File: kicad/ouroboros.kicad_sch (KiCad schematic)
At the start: 121 parts, among them J1 Eurorack Mono Jack, J10 Conn_01x03_Male, J11 Eurorack Mono Jack, J12 Eurorack Mono Jack, J13 Eurorack Mono Jack, J14 Eurorack Mono Jack, J19 Eurorack Mono Jack, J2 Eurorack Mono Jack, J20 Eurorack Mono Jack, J21 Eurorack Mono Jack, J22 Eurorack Mono Jack, J23 Eurorack Mono Jack, J24 Eurorack Mono Jack, J25 Eurorack Mono Jack, J26 Eurorack Mono Jack, J27 Eurorack Mono Jack, J28 Conn_01x06_Male, J29 Conn_01x04_Male, J3 Eurorack Mono Jack, J30 Conn_01x04_Male, J31 Conn_01x04_Male, J32 Conn_01x06_Male, J33 Conn_01x04_Male, J34 Conn_01x08_Male, J35 Conn_01x08_Male, J36 Eurorack Power Small, J38 Conn_02x04_Odd_Even, J4 Eurorack Mono Jack, J40 Conn_01x08_Female, J41 Conn_01x08_Female, J42 Conn_01x04_Female, J43 Conn_01x06_Female, J44 Conn_01x04_Female, J45 Conn_01x04_Female, J46 Conn_01x04_Female, J47 Conn_01x06_Female, J5 Eurorack Mono Jack, J6 Eurorack Mono Jack, J7 Eurorack Mono Jack, J8 Eurorack Mono Jack, J9 Eurorack Mono Jack, U1 TL074, U8 L78L05_TO92

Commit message: Updating pcb after tweaks
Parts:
- added R134: 100k, Rumblesan_Standard_Parts:R_Axial_DIN0207_L6.3mm_D2.5mm_P10.16mm_Horizontal, symbol Rumblesan_Standard_Parts:R
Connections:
- net VCC: now also R134.1; no longer RV20.1
- new net: R134.2, RV20.1
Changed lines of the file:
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@@
 	(wire
 		(pts
+			(xy 307.34 57.15) (xy 307.34 60.96)
+		)
+		(stroke
+			(width 0)
+			(type default)
+		)
+	)
+	(wire
+		(pts
 			(xy 200.66 45.72) (xy 200.66 95.25)
 		)
@@
 	(wire
 		(pts
-			(xy 307.34 58.42) (xy 307.34 60.96)
+			(xy 307.34 48.26) (xy 307.34 49.53)
 		)
 		(stroke
@@
 		)
 		(property "Name" "VCA Level CV"
-			(at 252.73 203.2 0)
+			(at 242.316 198.12 90)
 			(effects
 				(font
@@
 	(symbol
 		(lib_id "power:VCC")
-		(at 307.34 58.42 0)
+		(at 307.34 48.26 0)
 		(unit 1)
 		(exclude_from_sim no)
@@
 		(fields_autoplaced yes)
 		(property "Reference" "#PWR050"
-			(at 307.34 62.23 0)
+			(at 307.34 52.07 0)
 			(effects
 				(font
@@
 		)
 		(property "Value" "VCC"
-			(at 307.34 54.8442 0)
+			(at 307.34 44.6842 0)
 			(effects
 				(font
@@
 		)
 		(property "Footprint" ""
-			(at 307.34 58.42 0)
+			(at 307.34 48.26 0)
 			(effects
 				(font
@@
 		)
 		(property "Datasheet" ""
-			(at 307.34 58.42 0)
+			(at 307.34 48.26 0)
 			(effects
 				(font
@@
 		)
 		(property "Description" "Power symbol creates a global label with name \"VCC\""
-			(at 307.34 58.42 0)
+			(at 307.34 48.26 0)
 			(effects
 				(font
@@
 	)
 	(symbol
+		(lib_id "Rumblesan_Standard_Parts:R")
+		(at 307.34 53.34 0)
+		(mirror y)
+		(unit 1)
+		(exclude_from_sim no)
+		(in_bom yes)
+		(on_board yes)
+		(dnp no)
+		(property "Reference" "R134"
+			(at 300.228 53.086 0)
+			(effects
+				(font
+					(size 1.27 1.27)
+				)
+				(justify right)
+			)
+		)
+		(property "Value" "100k"
+			(at 300.228 51.308 0)
+			(effects
+				(font
+					(size 1.27 1.27)
+				)
+				(justify right)
+			)
+		)
+		(property "Footprint" "Rumblesan_Standard_Parts:R_Axial_DIN0207_L6.3mm_D2.5mm_P10.16mm_Horizontal"
+			(at 304.8 55.88 90)
+			(effects
+				(font
+					(size 1.27 1.27)
+				)
+				(hide yes)
+			)
+		)
+		(property "Datasheet" "~"
+			(at 300.99 53.34 90)
+			(effects
+				(font
+					(size 1.27 1.27)
+				)
+				(hide yes)
+			)
+		)
+		(property "Description" "Resistor"
+			(at 307.34 53.34 0)
+			(effects
+				(font
+					(size 1.27 1.27)
+				)
+				(hide yes)
+			)
+		)
+		(property "Tolerance" "1%"
+			(at 302.26 59.69 90)
+			(effects
+				(font
+					(size 1.27 1.27)
+				)
+				(hide yes)
+			)
+		)
+		(property "Power" "0.5W"
+			(at 302.26 45.72 90)
+			(effects
+				(font
+					(size 1.27 1.27)
+				)
+				(hide yes)
+			)
+		)
+		(property "Spec" "metal film"
+			(at 302.26 53.34 90)
+			(effects
+				(font
+					(size 1.27 1.27)
+				)
+				(hide yes)
+			)
+		)
+		(pin "1"
+		)
+		(pin "2"
+		)
+		(instances
+			(project "ouroboros"
+				(path "/5b0acaca-dc50-4fa5-b146-164c1b9ad031"
+					(reference "R134")
+					(unit 1)
+				)
+			)
+		)
+	)
+	(symbol
 		(lib_id "power:VEE")
 		(at 314.96 34.29 180)
@@
 		)
 		(property "Name" "VCA Output"
-			(at 247.65 160.02 0)
+			(at 233.426 157.48 90)
 			(effects
 				(font

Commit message: Updating with rev03 changes
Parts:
- removed J22: Eurorack Mono Jack, Rumblesan_Audio_Connectors:Jack_3.5mm_QingPu_WQP-PJ398SM_Vertical, symbol Connector_Audio:AudioJack2_SwitchT
- removed J38: Conn_02x04_Odd_Even, Connector_PinHeader_2.54mm:PinHeader_2x04_P2.54mm_Vertical, symbol Connector_Generic:Conn_02x04_Odd_Even
- removed R99: 100k, Rumblesan_Standard_Parts:R_Axial_DIN0207_L6.3mm_D2.5mm_P10.16mm_Horizontal, symbol Rumblesan_Standard_Parts:R
- added J22: Conn_02x04_Odd_Even, Connector_PinHeader_2.54mm:PinHeader_2x04_P2.54mm_Vertical, symbol Connector_Generic:Conn_02x04_Odd_Even
- added R103, R86, R87, R97: 330r, Rumblesan_Standard_Parts:R_Axial_DIN0207_L6.3mm_D2.5mm_P10.16mm_Horizontal, symbol Device:R
- added R93: 30k, Rumblesan_Standard_Parts:R_Axial_DIN0207_L6.3mm_D2.5mm_P10.16mm_Horizontal, symbol Rumblesan_Standard_Parts:R
- J36: value Eurorack Power Small -> Conn_02x05_Odd_Even; footprint Rumblesan_Eurorack_Power:Eurorack_PowerHeader_2x05_P2.54mm_Shrouded -> Rumblesan_Eurorack_Power:Eurorack_Power_IDC-Header_2x05_P2.54mm_Vertical
- TP14, TP2, TP3: Name (none) -> GND
- TP5: value FilterResCVTestPoint -> TestPoint; Name (none) -> Filter Res CV
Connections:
- net Delay/AUDIO_IN: now also J29.2 (Pin_2); no longer J29.3 (Pin_3)
- net Delay/DELAY_WET_OUT: now also J29.3 (Pin_3); no longer J29.2 (Pin_2)
- net Divider/SIGNAL: now also J33.4 (Pin_4); no longer J33.1 (Pin_1)
- net Filter CV/V/OCT: now also J22.6 (Pin_6)
- net Filter VCA/AUDIO_INPUT2: now also R93.2
- net Filter VCA/BANDPASS: now also R86.2, R97.1; no longer J32.6 (Pin_6)
- net Filter VCA/HIGHPASS: now also R103.1
- net Filter VCA/LOWPASS: now also R87.1
- net GND: now also J33.1 (Pin_1), J34.1 (Pin_1), J41.1 (Pin_1), J42.1 (Pin_1), J22.4 (Pin_4), J22.8 (Pin_8); no longer J33.4 (Pin_4), J42.4 (Pin_4)
- net at RV12.2: now also J46.2 (Pin_2); no longer J46.3 (Pin_3)
- net at R23.2: now also J42.4 (Pin_4); no longer J42.1 (Pin_1)
- net at J2.TN, R2.1: now also J46.3 (Pin_3); no longer J46.2 (Pin_2)
- net Filter CV/I_FREQ renamed Filter CV/CV_FREQ
- net Filter CV/I_RES renamed Filter CV/CV_RES
- net Filter VCA/I_VCA renamed Filter VCA/CV_VCA
- new net: J32.6 (Pin_6), R86.1
- new net: J22.1 (Pin_1), R87.2
- new net: J22.2 (Pin_2), R97.2
- new net: J22.3 (Pin_3), R93.1
- new net: J22.5 (Pin_5), R103.2
- new net EXTRA_MCU_PIN: J22.7 (Pin_7)
- no-connect marks 14 -> 12
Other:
- sheet Divider ports: added EXTRA_PIN; removed RESET
- sheet Filter CV ports: added CV_FREQ, CV_RES; removed I_FREQ, I_RES
- sheet Filter VCA ports: added CV_FREQ, CV_RES, CV_VCA; removed I_FREQ, I_RES, I_VCA
- sheet VCA CV ports: added CV_VCA; removed I_VCA
- moved on the sheet: TP10, TP9

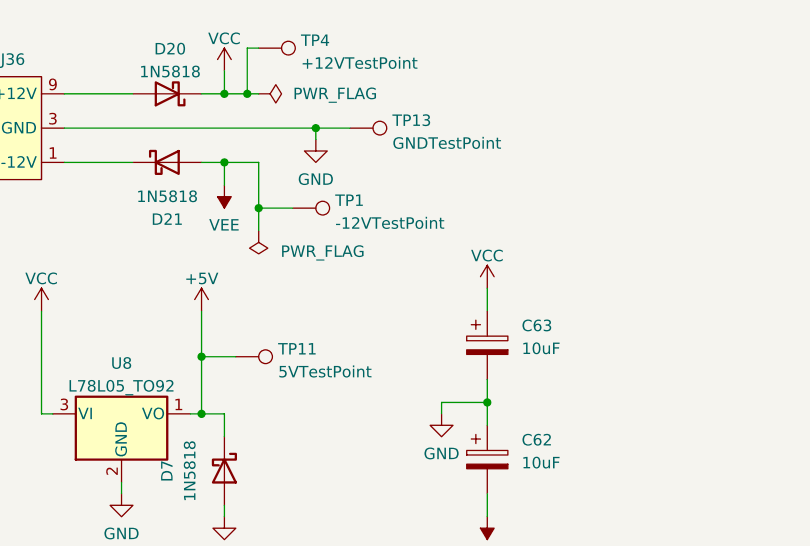
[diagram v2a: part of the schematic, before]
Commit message: Digital ground for divider and other layout improvements
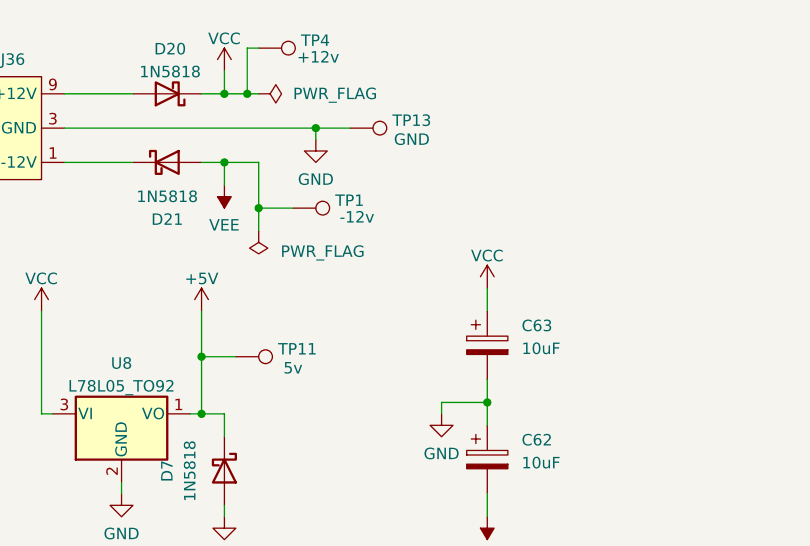
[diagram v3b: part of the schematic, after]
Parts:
- TP1: value -12VTestPoint -> TestPoint; Name (none) -> -12v
- TP11: value 5VTestPoint -> TestPoint
- TP13: value GNDTestPoint -> TestPoint; Name (none) -> GND
- TP4: value +12VTestPoint -> TestPoint; Name (none) -> +12v
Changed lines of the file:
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@@
 		(on_board yes)
 		(dnp no)
-		(fields_autoplaced yes)
 		(property "Reference" "TP4"
 			(at 376.809 15.6753 90)
@@
 			)
 		)
-		(property "Value" "+12VTestPoint"
+		(property "Value" "TestPoint"
 			(at 376.809 18.2122 90)
 			(effects
@@
 				)
 				(justify left)
+				(hide yes)
 			)
 		)
@@
 			)
 		)
+		(property "Name" "+12v"
+			(at 378.714 17.526 90)
+			(effects
+				(font
+					(size 1.27 1.27)
+				)
+			)
+		)
 		(pin "1"
 		)
@@
 		(on_board yes)
 		(dnp no)
-		(fields_autoplaced yes)
 		(property "Reference" "TP11"
 			(at 374.269 49.9653 90)
@@
 			)
 		)
-		(property "Value" "5VTestPoint"
+		(property "Value" "TestPoint"
 			(at 374.269 52.5022 90)
 			(effects
@@
 				)
 				(justify left)
+				(hide yes)
 			)
 		)
@@
 			)
 		)
-		(property "Description" ""
-			(at 369.57 50.8 0)
+		(property "Description" "5v"
+			(at 375.92 52.07 90)
 			(effects
 				(font
 					(size 1.27 1.27)
 				)
-				(hide yes)
 			)
 		)
@@
 		(on_board yes)
 		(dnp no)
-		(fields_autoplaced yes)
 		(property "Reference" "TP13"
 			(at 386.969 24.5653 90)
@@
 			)
 		)
-		(property "Value" "GNDTestPoint"
+		(property "Value" "TestPoint"
 			(at 386.969 27.1022 90)
 			(effects
@@
 				)
 				(justify left)
+				(hide yes)
 			)
 		)
@@
 			)
 		)
+		(property "Name" "GND"
+			(at 389.128 26.67 90)
+			(effects
+				(font
+					(size 1.27 1.27)
+				)
+			)
+		)
 		(pin "1"
 		)
@@
 		(on_board yes)
 		(dnp no)
-		(fields_autoplaced yes)
 		(property "Reference" "TP1"
 			(at 380.619 33.4553 90)
@@
 			)
 		)
-		(property "Value" "-12VTestPoint"
+		(property "Value" "TestPoint"
 			(at 380.619 35.9922 90)
 			(effects
@@
 				)
 				(justify left)
+				(hide yes)
 			)
 		)
@@
 			)
 		)
+		(property "Name" "-12v"
+			(at 383.032 35.306 90)
+			(effects
+				(font
+					(size 1.27 1.27)
+				)
+			)
+		)

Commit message: More layout tweaks
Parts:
- TP7: value VCACVTestPoint -> TestPoint; Name (none) -> VCA CV
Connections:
- net Filter VCA/AUDIO_INPUT1: now also J32.4 (Pin_4); no longer J32.5 (Pin_5)
- net Filter VCA/VCA_INPUT: now also J32.6 (Pin_6); no longer J32.2 (Pin_2)
- net VCA CV/VCA_CV_ATTV_BOTTOM: now also J32.2 (Pin_2); no longer J32.3 (Pin_3)
- net VCA CV/VCA_LEVEL: now also J32.3 (Pin_3); no longer J32.4 (Pin_4)
- net at R86.1: now also J32.5 (Pin_5); no longer J32.6 (Pin_6)
- net at R24.2: now also J10.2 (Pin_2); no longer J10.1 (Pin_1)
- net at C6.2, R18.2, R22.2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: now also J10.3 (Pin_3); no longer J10.2 (Pin_2)
- net at J12.TN: now also J43.5 (Pin_5); no longer J43.6 (Pin_6)
- net at J43.2 (Pin_2): now also RV11.1; no longer J7.T
- net at J43.3 (Pin_3): now also RV14.2; no longer RV11.1
- net at J43.4 (Pin_4): now also J11.TN; no longer RV14.2
- new net: J43.6 (Pin_6), J7.T
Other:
- moved on the sheet: RV14
